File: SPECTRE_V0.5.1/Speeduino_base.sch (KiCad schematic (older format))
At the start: 213 parts, among them J1 Conn_01x06_Male, J2 Conn_02x04_Odd_Even, Q1 AO3400, Q10 AO3401A, Q11 AO3401A, Q12 BSP78, Q13 BSP78, Q14 BSP78, Q15 BSP78, Q16 AO3422, Q17 AO3422, Q18 BSP78, Q19 BSP78, Q2 AO3400, Q20 BSP78, Q21 AO3401A, Q22 AO3401A, Q23 BSP78, Q24 BSP78, Q25 BSP78, Q26 BSP78, Q3 AO3400, Q4 AO3400, Q5 AO3400, Q6 AO3400, Q7 AO3400, Q8 AO3422, Q9 AO3422, U1 MAX9926UAEE+, U2 LM78M05_TO220, U3 TL431DBZ, U4 molex_48pin, U5 TJA1050, U6 MAX3232

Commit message: clean-up board V0.5 started on board V0.5.1
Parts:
- removed D27, D28, D32, D33: 1N4007, Diode_SMD:D_SMA, symbol Device:D_Schottky_Small
- removed Q10, Q11, Q21, Q22: AO3401A, Package_TO_SOT_SMD:SOT-23_Handsoldering, symbol Transistor_FET:AO3401A
- removed Q16, Q17, Q8, Q9: AO3422, Package_TO_SOT_SMD:SOT-23_Handsoldering, symbol speeduino_lib:SMD-MOSFET-N-CH-30V-5.8A-AO3400(SOT-23)
- removed R73, R74, R86, R87: 1k, Speeduino_base:R0603, symbol Device:R_Small
- removed R76, R77, R91, R92: 1k8, Speeduino_base:R0603, symbol Device:R_Small
- removed R78, R79, R96, R97: 470R, Speeduino_base:R0603, symbol Device:R_Small
- added C31, C32: 1000uF, Capacitor_SMD:CP_Elec_10x12.5, symbol Device:CP_Small
- added D34, D35: BAT54S, Speeduino_base:SOT23, symbol Speeduino_base-eagle-import:BAT54S
- added D36, D37: 1N4007, Diode_SMD:D_SMA, symbol Device:D_Small
- added Q27, Q28: AO3400, Speeduino_base:SOT-23, symbol Speeduino_base-eagle-import:SMD-MOSFET-N-CH-20V-2.1A-CJ2302(SOT-23)
- added R100, R101, R104, R105: 1k, Speeduino_base:R0603, symbol Speeduino_base-eagle-import:SMD-RES-470R-5%-1_10W(0603)
- added R102, R103: 100R, Speeduino_base:R0603, symbol Speeduino_base-eagle-import:SMD-RES-470R-5%-1_10W(0603)
- added R106, R107: 10k, Speeduino_base:R0603, symbol Speeduino_base-eagle-import:SMD-RES-470R-5%-1_10W(0603)
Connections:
- net labels added: AIN_0, D0, D1, Spare_1-Out, Spare_2-Out
- net labels removed: AIN_3
- wire segments 570 -> 561
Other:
- moved on the sheet: D24, D25, D26, JP10, JP11, JP8, Q1, Q3, Q4, Q6, R37, R40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

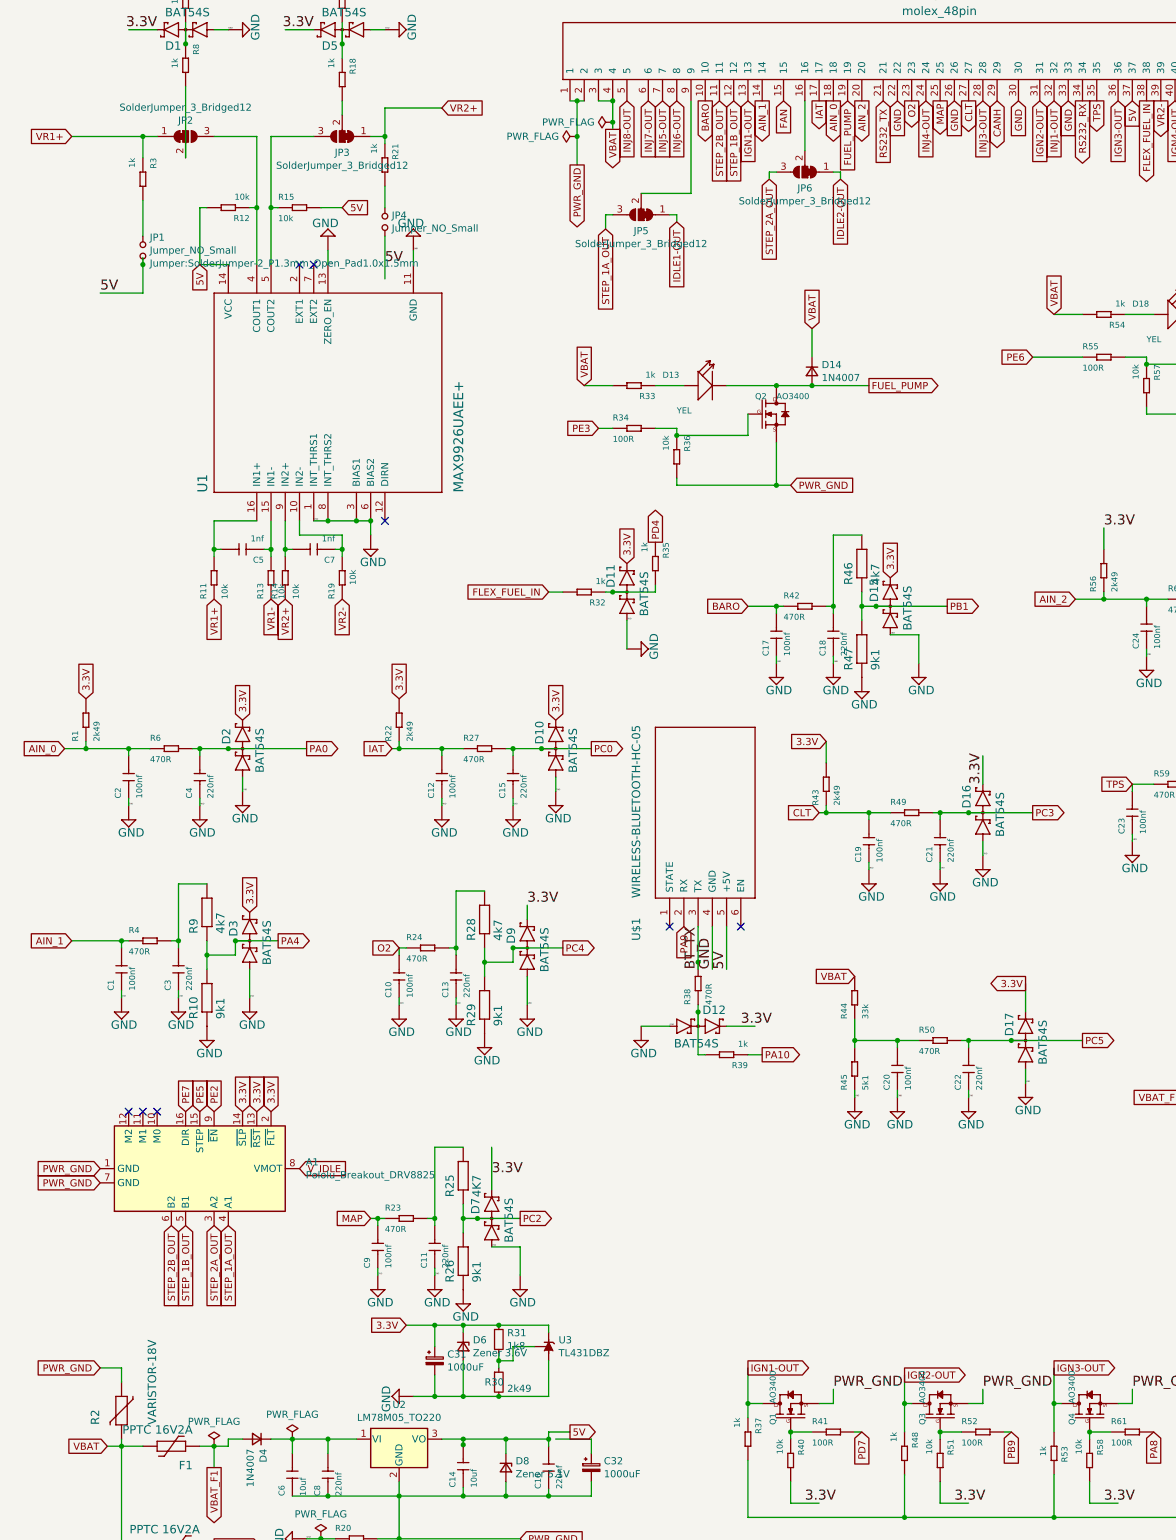
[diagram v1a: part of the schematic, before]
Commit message: re-add bluetooth module
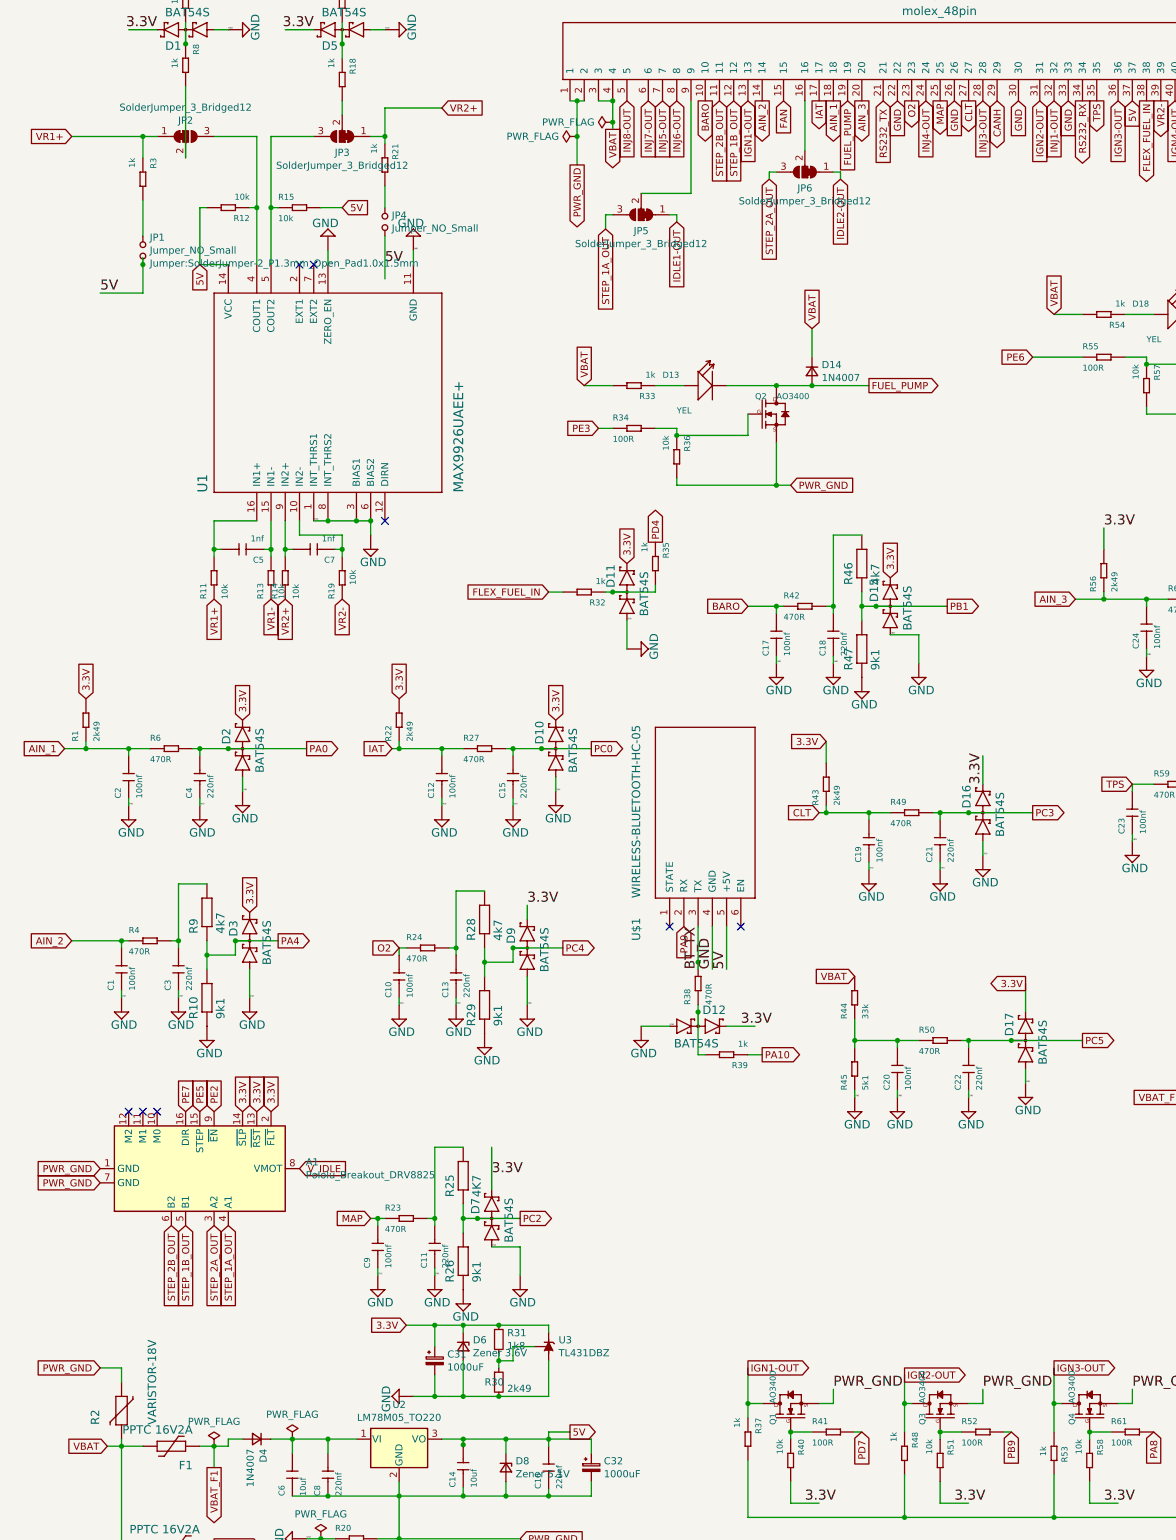
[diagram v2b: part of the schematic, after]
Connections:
- net labels added: AIN_3
- net labels removed: AIN_0
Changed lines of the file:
@@
 Text GLabel 9050 1400 3    50   Input ~ 0
 TACHO-OUT
-Text GLabel 5250 1400 3    50   Output ~ 0
-AIN_1
-Text GLabel 5750 1400 3    50   Output ~ 0
-AIN_0
 $Comp
 L Jumper:SolderJumper_3_Bridged12 JP6
@@
 Connection ~ 750  7300
 Text GLabel 400  7300 0    50   Input ~ 0
-AIN_1
+AIN_2
 Text GLabel 1650 7100 1    50   Input ~ 0
 3.3V
@@
 PC5
 Text GLabel 350  5950 0    50   Input ~ 0
-AIN_0
+AIN_1
 Wire Wire Line
 	350  5950 500  5950
@@
 IGN4-OUT
 Text GLabel 7450 4900 0    50   Input ~ 0
-AIN_2
+AIN_3
 Wire Wire Line
 	7450 4900 7650 4900
@@
 PC7
 Text GLabel 5950 1400 3    50   Output ~ 0
-AIN_2
+AIN_3
 NoConn ~ 10500 4800
 NoConn ~ 10500 4900
@@
 $EndComp
 Wire Wire Line
-	3800 10800 4050 10800
-Wire Wire Line
 	4050 10800 4050 10900
 Wire Wire Line
@@
 Wire Wire Line
 	9050 11400 8350 11400
+Text GLabel 5250 1400 3    50   Output ~ 0
+AIN_2
+Text GLabel 5750 1400 3    50   Output ~ 0
+AIN_1
+Wire Wire Line
+	3750 10800 4050 10800
 $EndSCHEMATC

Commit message: Clean-up PCB V0.5.1
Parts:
- removed D34, D35: BAT54S, Speeduino_base:SOT23, symbol Speeduino_base-eagle-import:BAT54S
- removed R100, R101, R104, R105: 1k, Speeduino_base:R0603, symbol Speeduino_base-eagle-import:SMD-RES-470R-5%-1_10W(0603)
- added D27: YEL, Speeduino_base:LED-0603, symbol Speeduino_base-eagle-import:SMD-LED-CLEAR-YELLOW(0603)
- added JP14, JP15: SolderJumper_3_Bridged12, Jumper:SolderJumper-3_P1.3mm_Bridged12_Pad1.0x1.5mm, symbol Jumper:SolderJumper_3_Bridged12
- added Q8: AO3400, Speeduino_base:SOT-23, symbol Speeduino_base-eagle-import:SMD-MOSFET-N-CH-20V-2.1A-CJ2302(SOT-23)
- added R73: 100R, Speeduino_base:R0603, symbol Speeduino_base-eagle-import:SMD-RES-470R-5%-1_10W(0603)
- C31, C32: value 1000uF -> 470uF 6.3V; footprint Capacitor_SMD:CP_Elec_10x12.5 -> Capacitor_SMD:CP_Elec_6.3x7.7
- R25: value 4K7 -> 4k7
- R33, R54: value 1k -> 470R
- U2: footprint Package_TO_SOT_THT:TO-220-3_Vertical -> Package_TO_SOT_THT:TO-220-3_Horizontal_TabUp
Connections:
- net labels added: PA6
- net labels removed: D0, D1
- wire segments 561 -> 573
- no-connect marks 51 -> 50
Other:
- moved on the sheet: JP10, JP11, JP5, JP6

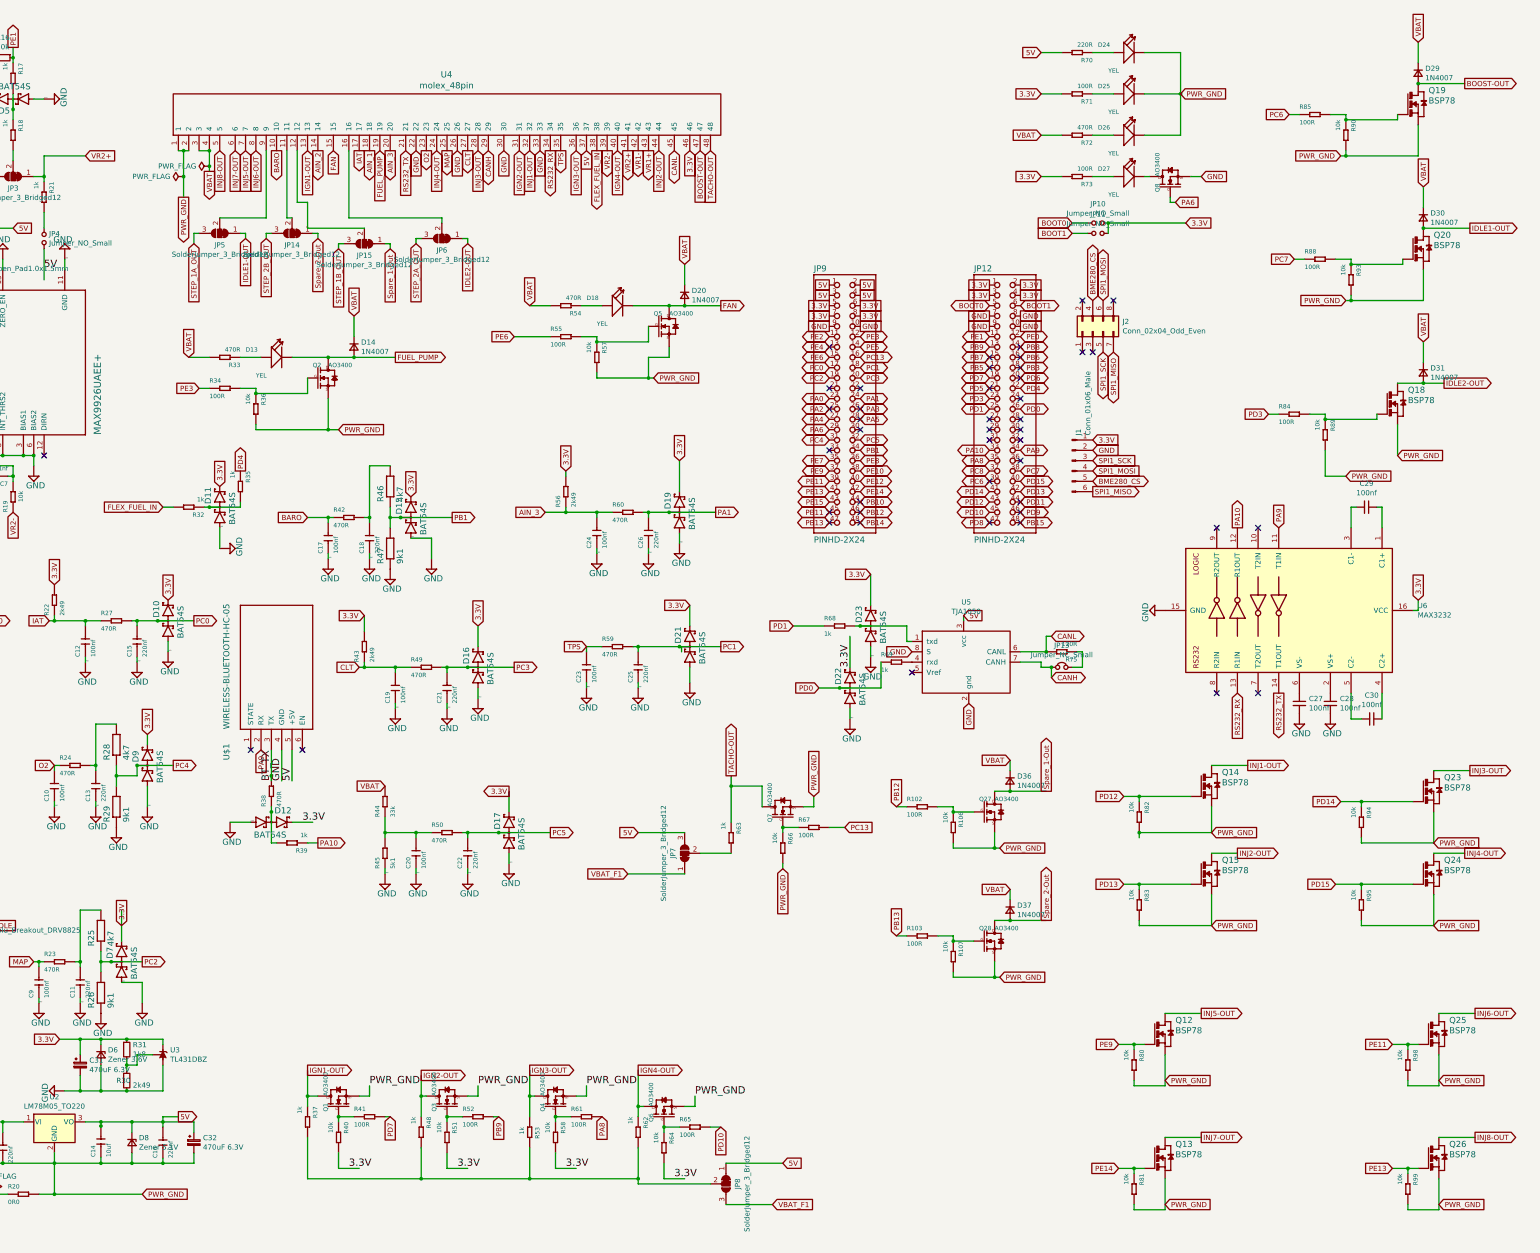
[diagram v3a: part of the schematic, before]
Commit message: Renumbered all parts from start
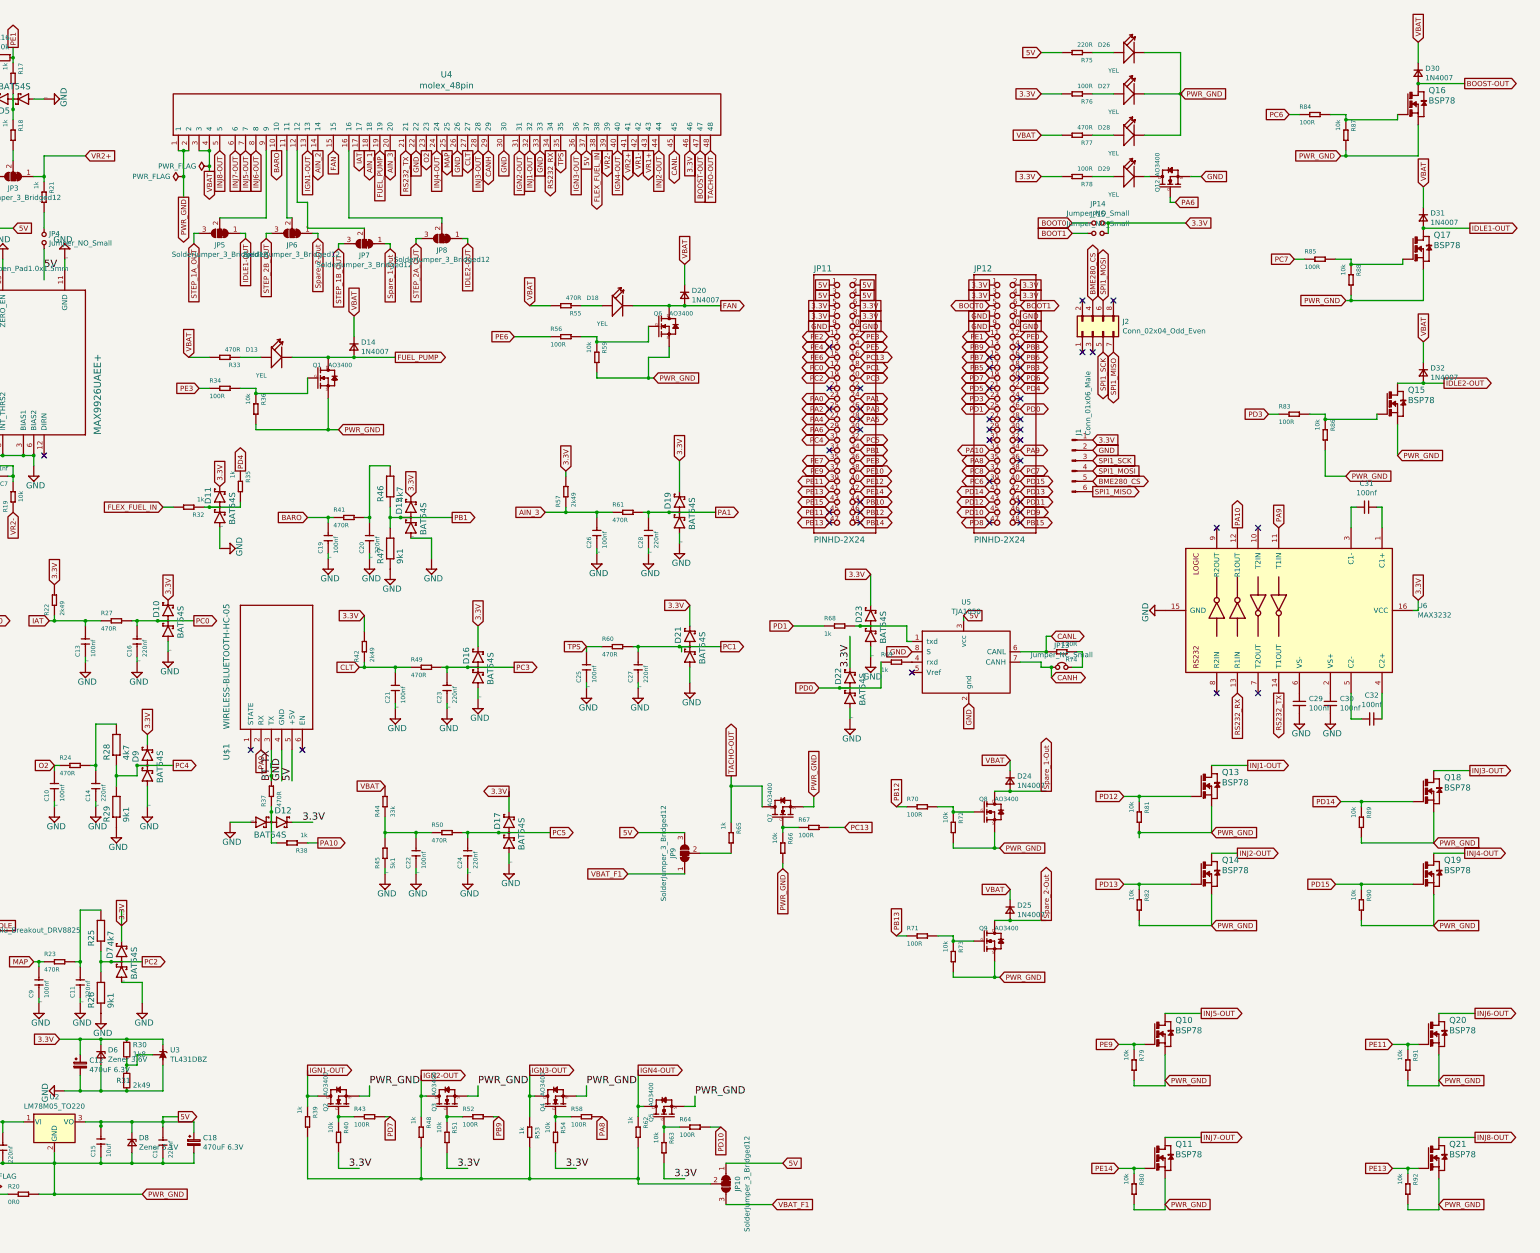
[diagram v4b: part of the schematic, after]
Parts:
- renumbered C31 to C12, C12 to C13, C13 to C14, C14 to C15, C15 to C16, C16 to C17, C32 to C18, C17 to C19, C18 to C20, C19 to C21, C20 to C22, C21 to C23, C22 to C24, C23 to C25, C24 to C26, C25 to C27, C26 to C28, C27 to C29, C28 to C30, C29 to C31, C30 to C32, D36 to D24, D37 to D25, D24 to D26, D25 to D27, D26 to D28, D27 to D29, D29 to D30, D30 to D31, D31 to D32, JP8 to JP10, JP9 to JP11, JP10 to JP14, JP11 to JP15, JP14 to JP6, JP15 to JP7, JP6 to JP8, JP7 to JP9, Q2 to Q1, Q12 to Q10, Q13 to Q11, Q8 to Q12, Q14 to Q13, Q15 to Q14, Q18 to Q15, Q19 to Q16, Q20 to Q17, Q23 to Q18, Q24 to Q19, Q1 to Q2, Q25 to Q20, Q26 to Q21, Q6 to Q5, Q5 to Q6, Q27 to Q8, Q28 to Q9, R31 to R30, R30 to R31, R38 to R37, R39 to R38, R37 to R39, R42 to R41, R43 to R42, R41 to R43, R58 to R54, R54 to R55, R55 to R56, R56 to R57, R61 to R58, R57 to R59, R59 to R60, R60 to R61, R64 to R63, R65 to R64, R63 to R65, R102 to R70, R103 to R71, R106 to R72, R107 to R73, R75 to R74, R70 to R75, R71 to R76, R72 to R77, R73 to R78, R80 to R79, R81 to R80, R82 to R81, R83 to R82, R84 to R83, R85 to R84, R88 to R85, R89 to R86, R90 to R87, R93 to R88, R94 to R89, R95 to R90, R98 to R91, R99 to R92

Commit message: update molex 48 pin to correct location
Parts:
- U4: footprint rusefi_lib:Molex_48 -> Speeduino_base:Molex_48; symbol molex_48pin:molex_48pin -> speeduino_lib:molex_48pin
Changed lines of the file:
@@
 Connection ~ 4200 1400
 $Comp
-L molex_48pin:molex_48pin U4
+L speeduino_lib:molex_48pin U4
 U 1 1 5E17AB54
 P 6900 1950
 F 0 "U4" V 8187 2355 60  0000 C CNN
 F 1 "molex_48pin" V 8081 2355 60  0000 C CNN
-F 2 "rusefi_lib:Molex_48" H 6900 1950 60  0001 C CNN
+F 2 "Speeduino_base:Molex_48" H 6900 1950 60  0001 C CNN
 F 3 "" H 6900 1950 60  0001 C CNN
 	1    6900 1950
